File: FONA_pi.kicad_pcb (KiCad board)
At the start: 2 copper layers, 88.4 x 59.1 mm, 35 parts, among them J1 Conn_01x20_Socket, J10 Conn_01x04_Pin, J11 Conn_01x20_Socket, J12 Conn_01x20_Socket, J13 Conn_01x06_Socket, J14 Conn_01x06_Socket, J15 Conn_01x06_Socket, J16 Conn_01x06_Socket, J17 Conn_01x06_Socket, J18 Conn_01x04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

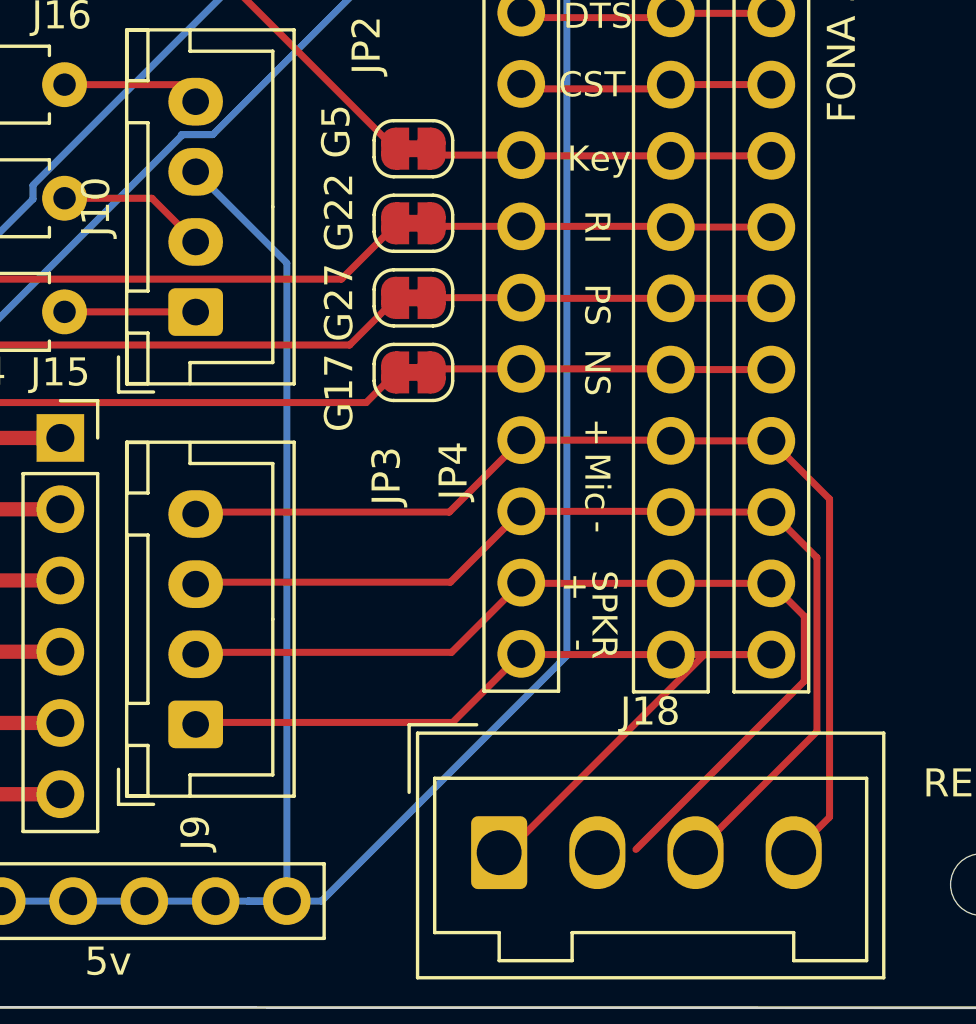
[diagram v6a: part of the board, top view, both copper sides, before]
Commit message: Fixed DRC errors
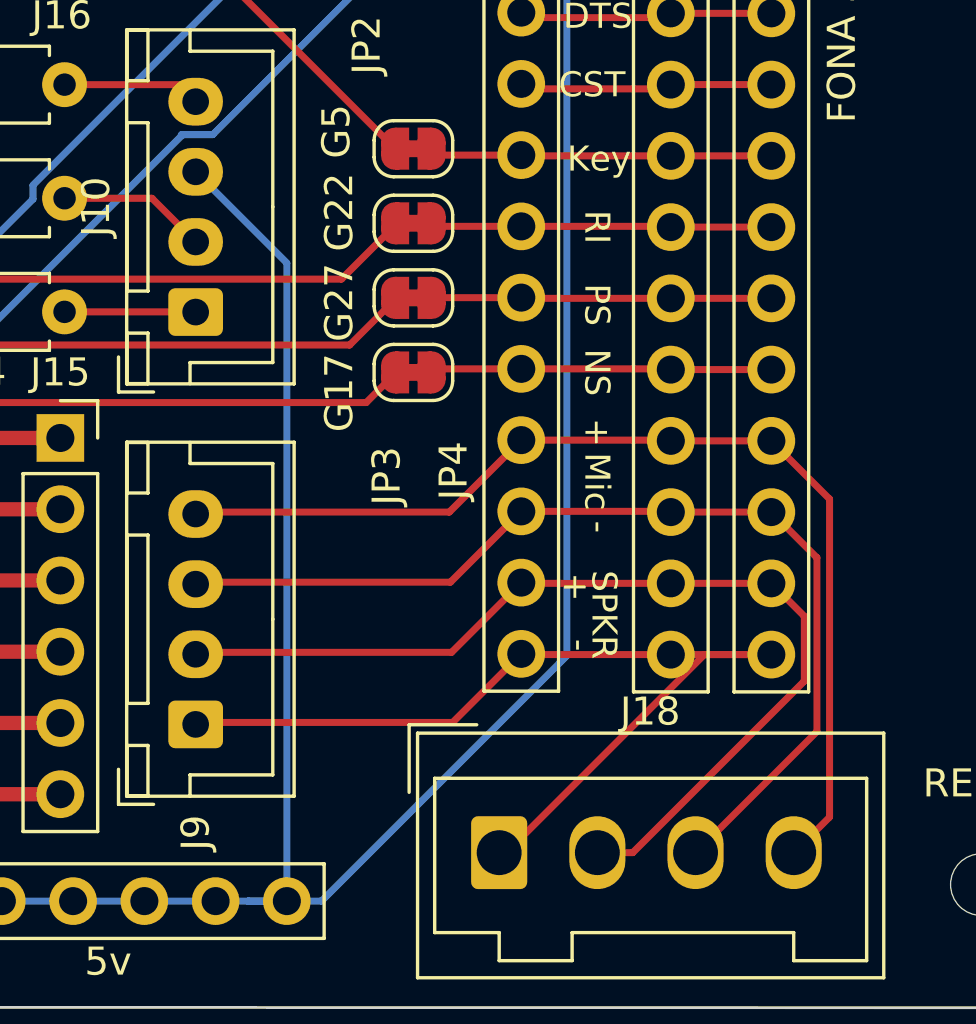
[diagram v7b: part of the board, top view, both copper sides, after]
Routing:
- net Net-(J18-Pin_2): track 33.2 -> 34.6 mm
- net Net-(J10-Pin_3): track 125.6 -> 124.8 mm
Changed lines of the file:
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@@
       (outputformat 1)
       (mirror false)
-      (drillshape 1)
+      (drillshape 0)
       (scaleselection 1)
-      (outputdirectory "")
+      (outputdirectory "gerbers")
     )
   )
@@
     (fp_line (start 9.95 3.4) (end 9.95 -2.35)
       (stroke (width 0.1) (type solid)) (layer "F.Fab"))
-    (pad "1" thru_hole roundrect (at 0 0 90) (size 1.7 1.95) (drill 0.95) (layers "*.Cu" "*.Mask") (roundrect_rratio 0.147059)
+    (pad "1" thru_hole roundrect (at 0 0 90) (size 1.7 1.95) (drill 0.95) (layers "*.Cu" "*.Mask") (roundrect_rratio 0.1470588235)
       (net 32 "Net-(J18-Pin_1)") (pinfunction "Pin_1") (pintype "passive"))
     (pad "2" thru_hole oval (at 2.5 0 90) (size 1.7 1.95) (drill 0.95) (layers "*.Cu" "*.Mask")
@@
     (fp_line (start 9.95 3.4) (end 9.95 -2.35)
       (stroke (width 0.1) (type solid)) (layer "F.Fab"))
-    (pad "1" thru_hole roundrect (at 0 0 90) (size 1.7 1.95) (drill 0.95) (layers "*.Cu" "*.Mask") (roundrect_rratio 0.147059)
+    (pad "1" thru_hole roundrect (at 0 0 90) (size 1.7 1.95) (drill 0.95) (layers "*.Cu" "*.Mask") (roundrect_rratio 0.1470588235)
       (net 30 "Net-(J10-Pin_1)") (pinfunction "Pin_1") (pintype "passive"))
     (pad "2" thru_hole oval (at 2.5 0 90) (size 1.7 1.95) (drill 0.95) (layers "*.Cu" "*.Mask")
@@
   (segment (start 137.16 101.56) (end 145.4296 101.56) (width 0.25) (layer "F.Cu") (net 61))
   (segment (start 153.2864 101.6) (end 147.9804 101.6) (width 0.25) (layer "F.Cu") (net 62))
+  (segment (start 158.0454 105.0838) (end 151.928 111.2012) (width 0.25) (layer "F.Cu") (net 62))
   (segment (start 158.0454 105.0838) (end 158.0454 102.775) (width 0.25) (layer "F.Cu") (net 62))
   (segment (start 156.8704 101.6) (end 153.2864 101.6) (width 0.25) (layer "F.Cu") (net 62))
+  (segment (start 151.928 111.2012) (end 150.6676 111.2012) (width 0.25) (layer "F.Cu") (net 62))
   (segment (start 147.955 101.5746) (end 145.4696 104.06) (width 0.25) (layer "F.Cu") (net 62))
   (segment (start 158.0454 102.775) (end 156.8704 101.6) (width 0.25) (layer "F.Cu") (net 62))
-  (segment (start 152.0425 111.0867) (end 158.0454 105.0838) (width 0.25) (layer "F.Cu") (net 62))
   (segment (start 145.4696 104.06) (end 137.16 104.06) (width 0.25) (layer "F.Cu") (net 62))
   (segment (start 116.2304 109.22) (end 112.649 109.22) (width 0.508) (layer "F.Cu") (net 63))
@@
   (segment (start 123.6472 112.9284) (end 119.8626 109.1438) (width 0.25) (layer "B.Cu") (net 63))
   (segment (start 139.5984 90.1808) (end 136.3472 86.9296) (width 0.25) (layer "B.Cu") (net 63))
-  (segment (start 136.3472 86.9296) (end 136.9272 87.5096) (width 0.25) (layer "B.Cu") (net 63))
   (segment (start 138.22 112.9284) (end 137.0584 112.9284) (width 0.25) (layer "B.Cu") (net 63))
   (segment (start 127.9678 96.4184) (end 124.3838 96.4184) (width 0.508) (layer "F.Cu") (net 64))
